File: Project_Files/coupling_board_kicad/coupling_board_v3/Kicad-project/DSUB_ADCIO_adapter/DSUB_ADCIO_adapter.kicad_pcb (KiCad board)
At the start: 2 copper layers, 36.1 x 70 mm, 6 parts, among them J1 Conn_02x04_Odd_Even, J10 Conn_02x12_Odd_Even, J2 Conn_02x04_Odd_Even, J3 Conn_02x04_Odd_Even, J4 Conn_02x12_Odd_Even, J6 DB25_Socket

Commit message: Updated design
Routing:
- net GND1: track 0.00 -> 11.0 mm, vias 0 -> 4
- net 3V3_VCUT: track 97.3 -> 98.4 mm

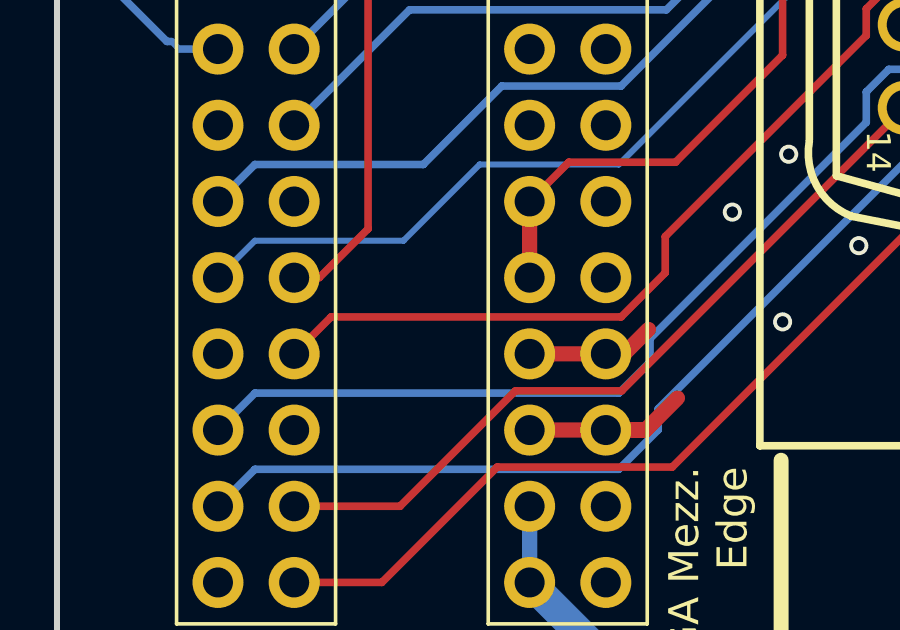
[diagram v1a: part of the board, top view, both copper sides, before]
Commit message: Committing prototyped DRC checked version
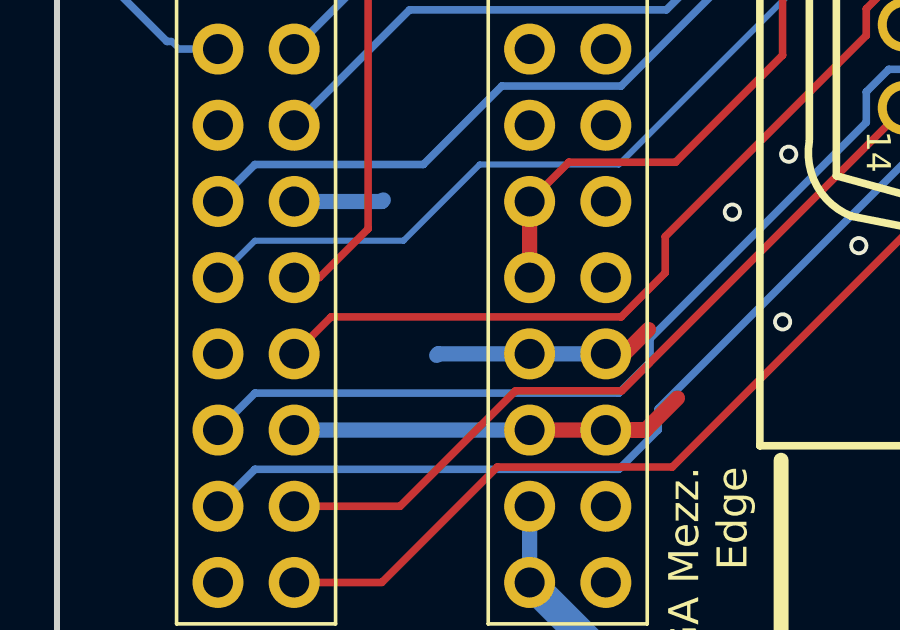
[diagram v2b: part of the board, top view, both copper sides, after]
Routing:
- net GND1: track 11.0 -> 25.0 mm
